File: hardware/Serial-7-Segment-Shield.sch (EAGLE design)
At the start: 28 parts, among them U1 ARDUINO_SHIELDLABEL

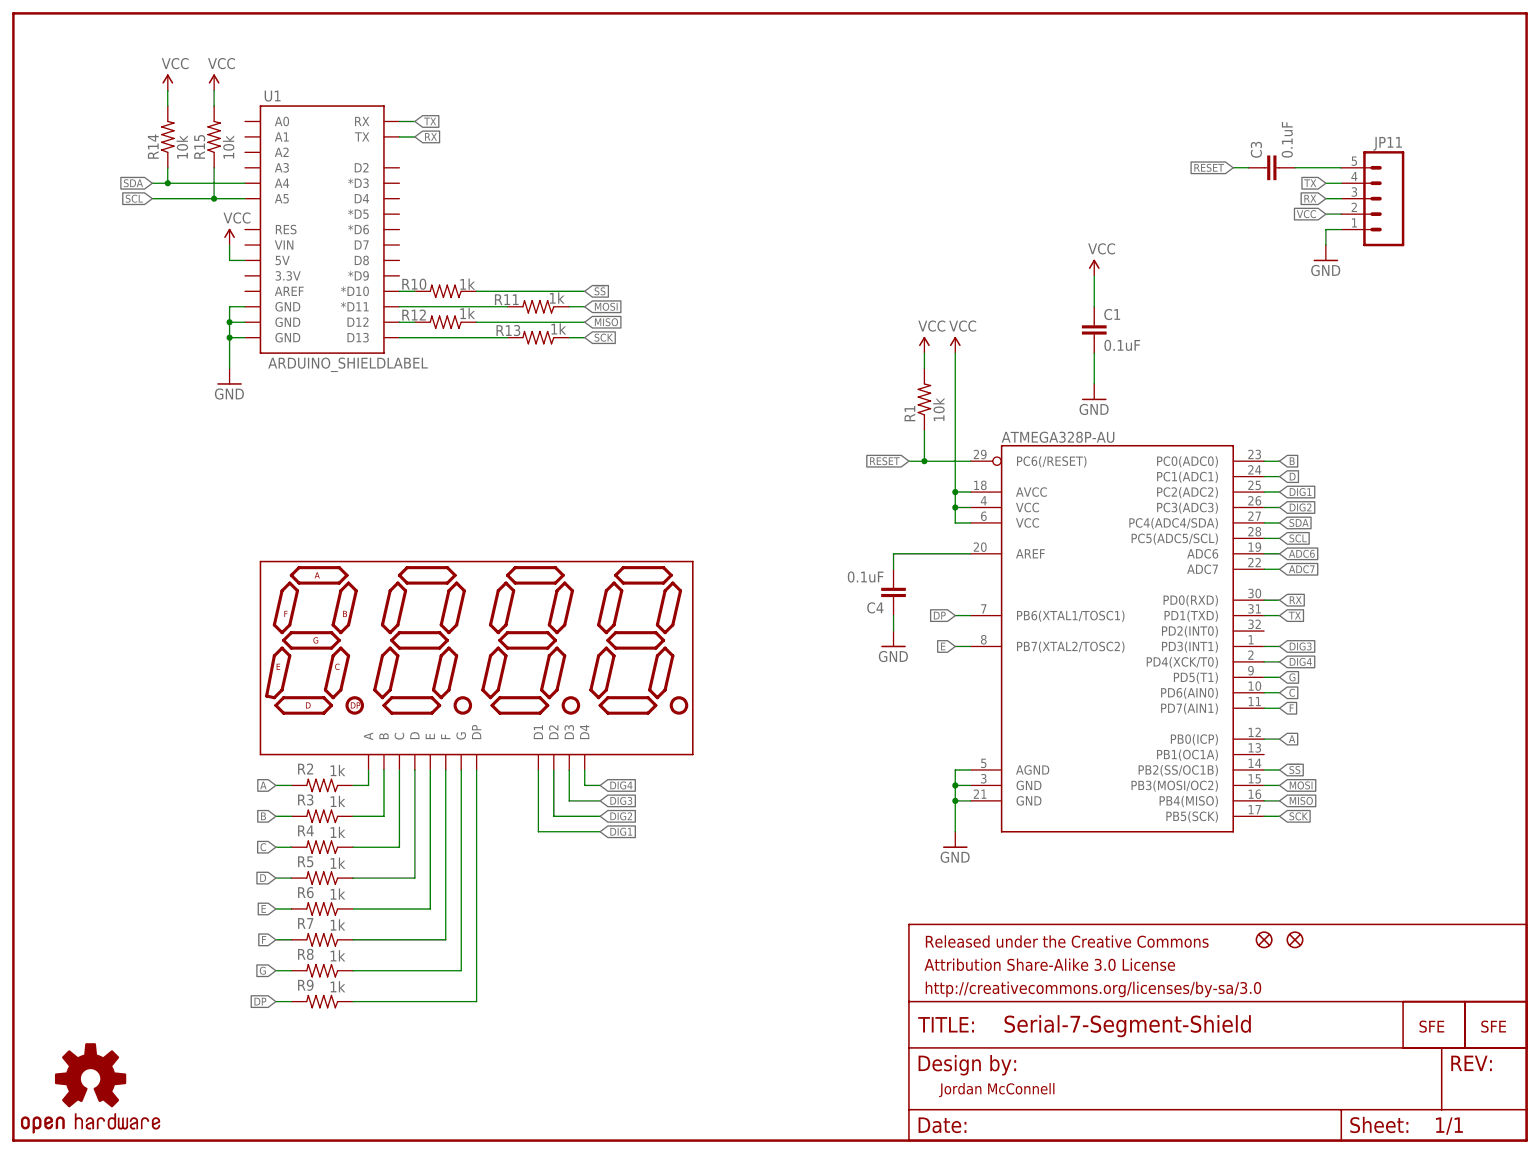
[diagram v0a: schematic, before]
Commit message: Updated hardware to v02.
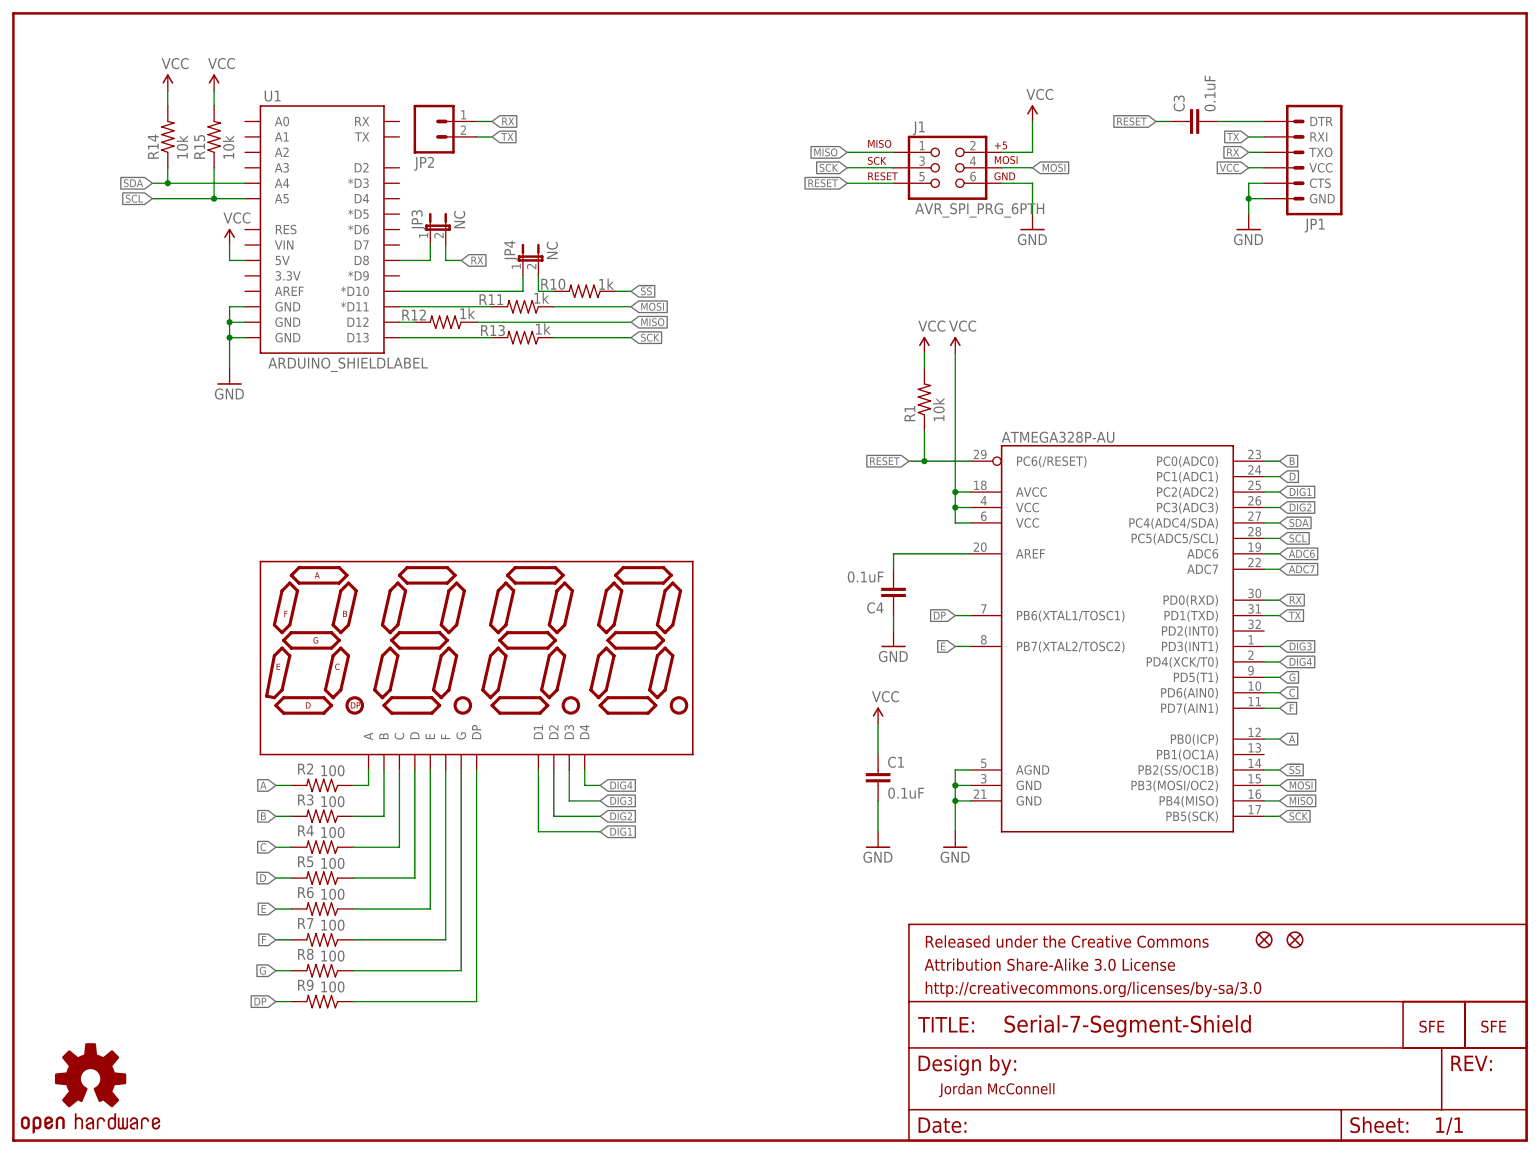
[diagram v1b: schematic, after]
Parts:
- removed JP11: (no value), SparkFun-Connectors:M05PTH-NS
- added J1: AVR_SPI_PRG_6PTH, SparkFun-Connectors:AVR_SPI_PRG_6PTH
- added JP1: (no value), SparkFun-Connectors:ARDUINO_SERIAL_PROGRAMPTH
- added JP2: (no value), SparkFun-Connectors:M02PTH
- added JP3, JP4: NC, SparkFun-Passives:JUMPER-2SMD-NC
- R2, R3, R4, R5, R6, R7, R8, R9: value 1k -> 100
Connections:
- new net N$6: JP4.1, U1.*D10
- new net N$7: JP3.1, U1.D8
- net GND: now also J1.6, JP1.CTS, JP1.GND; no longer JP11.1
- net MISO: now also J1.1
- net MOSI: now also J1.4
- net N$13: now also JP1.DTR; no longer JP11.5
- net N$5: now also JP4.2; no longer U1.*D10
- net RESET: now also J1.5
- net RX: now also JP1.TXO, JP2.1, JP3.2; no longer JP11.3, U1.TX
- net SCK: now also J1.3
- net TX: now also JP1.RXI, JP2.2; no longer JP11.4, U1.RX
- net VCC: now also J1.2, JP1.VCC; no longer JP11.2
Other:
- moved on the sheet: C1, C3, R10, R11, R13

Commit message: Minor update to v02, now includes color selection silk.
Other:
- note added: "v02"
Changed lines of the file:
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@@
 <plain>
 <text x="152.4" y="7.62" size="1.778" layer="94">Jordan McConnell</text>
+<text x="238.76" y="7.62" size="1.778" layer="94">v02</text>
 </plain>
 <instances>

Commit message: v10 Production Ready files
Change version number on boards to v10
Created board panel for manufacture
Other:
- note added: "v10"
- note removed: "v02"
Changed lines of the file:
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@@
 <?xml version="1.0" encoding="utf-8"?>
 <!DOCTYPE eagle SYSTEM "eagle.dtd">
-<eagle version="6.2">
+<eagle version="6.4">
 <drawing>
 <settings>
@@
 <plain>
 <text x="152.4" y="7.62" size="1.778" layer="94">Jordan McConnell</text>
-<text x="238.76" y="7.62" size="1.778" layer="94">v02</text>
+<text x="238.76" y="7.62" size="1.778" layer="94">v10</text>
 </plain>
 <instances>

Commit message: 0603 Cap/Res Change
Changed all caps and res to 0603, minor trace re-routing
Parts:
- C1: device SparkFun:CAP0402-CAP -> SparkFun:CAP0603-CAP
- C3, C4: device SparkFun-Passives:CAP0402-CAP -> SparkFun-Passives:CAP0603-CAP
- R1, R10, R11, R12, R13, R14, R15, R2, R3, R4, R5, R6, R7, R8, R9: device SparkFun:RESISTOR0402-RES -> SparkFun:RESISTOR0603-RES
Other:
- note added: "v11"
- note removed: "v10"
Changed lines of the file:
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@@
 <?xml version="1.0" encoding="utf-8"?>
 <!DOCTYPE eagle SYSTEM "eagle.dtd">
-<eagle version="6.4">
+<eagle version="6.5.0">
 <drawing>
 <settings>
@@
 <layer number="18" name="Vias" color="2" fill="1" visible="no" active="no"/>
 <layer number="19" name="Unrouted" color="6" fill="1" visible="no" active="no"/>
-<layer number="20" name="Dimension" color="15" fill="1" visible="no" active="no"/>
-<layer number="21" name="tPlace" color="16" fill="1" visible="no" active="no"/>
-<layer number="22" name="bPlace" color="14" fill="1" visible="no" active="no"/>
+<layer number="20" name="Dimension" color="6" fill="1" visible="no" active="no"/>
+<layer number="21" name="tPlace" color="6" fill="1" visible="no" active="no"/>
+<layer number="22" name="bPlace" color="6" fill="1" visible="no" active="no"/>
 <layer number="23" name="tOrigins" color="15" fill="1" visible="no" active="no"/>
 <layer number="24" name="bOrigins" color="15" fill="1" visible="no" active="no"/>
@@
 <part name="GND1" library="SparkFun" deviceset="GND" device=""/>
 <part name="P+2" library="SparkFun" deviceset="VCC" device=""/>
-<part name="R1" library="SparkFun" deviceset="RESISTOR" device="0402-RES" value="10k"/>
-<part name="C1" library="SparkFun" deviceset="CAP" device="0402-CAP" value="0.1uF"/>
+<part name="R1" library="SparkFun" deviceset="RESISTOR" device="0603-RES" value="10k"/>
+<part name="C1" library="SparkFun" deviceset="CAP" device="0603-CAP" value="0.1uF"/>
 <part name="P+3" library="SparkFun" deviceset="VCC" device=""/>
 <part name="GND4" library="SparkFun" deviceset="GND" device=""/>
 <part name="GND7" library="SparkFun-Aesthetics" deviceset="GND" device=""/>
-<part name="C3" library="SparkFun-Passives" deviceset="CAP" device="0402-CAP" value="0.1uF"/>
+<part name="C3" library="SparkFun-Passives" deviceset="CAP" device="0603-CAP" value="0.1uF"/>
 <part name="U$4" library="SparkFun-Aesthetics" deviceset="OSHW-LOGO" device="S"/>
-<part name="C4" library="SparkFun-Passives" deviceset="CAP" device="0402-CAP" value="0.1uF"/>
+<part name="C4" library="SparkFun-Passives" deviceset="CAP" device="0603-CAP" value="0.1uF"/>
 <part name="GND2" library="SparkFun" deviceset="GND" device=""/>
 <part name="JP9" library="SparkFun" deviceset="FIDUCIAL" device="UFIDUCIAL"/>
@@
 <part name="LOGO2" library="SparkFun-Aesthetics" deviceset="LOGO-SFE" device="NEW"/>
 <part name="U$1" library="SparkFun-Displays" deviceset="7-SEGMENT-4DIGIT-COUNTER" device="PTH"/>
-<part name="R2" library="SparkFun" deviceset="RESISTOR" device="0402-RES" value="100"/>
-<part name="R3" library="SparkFun" deviceset="RESISTOR" device="0402-RES" value="100"/>
-<part name="R4" library="SparkFun" deviceset="RESISTOR" device="0402-RES" value="100"/>
-<part name="R5" library="SparkFun" deviceset="RESISTOR" device="0402-RES" value="100"/>
-<part name="R6" library="SparkFun" deviceset="RESISTOR" device="0402-RES" value="100"/>
-<part name="R7" library="SparkFun" deviceset="RESISTOR" device="0402-RES" value="100"/>
-<part name="R8" library="SparkFun" deviceset="RESISTOR" device="0402-RES" value="100"/>
-<part name="R9" library="SparkFun" deviceset="RESISTOR" device="0402-RES" value="100"/>
-<part name="R10" library="SparkFun" deviceset="RESISTOR" device="0402-RES" value="1k"/>
-<part name="R11" library="SparkFun" deviceset="RESISTOR" device="0402-RES" value="1k"/>
-<part name="R12" library="SparkFun" deviceset="RESISTOR" device="0402-RES" value="1k"/>
-<part name="R13" library="SparkFun" deviceset="RESISTOR" device="0402-RES" value="1k"/>
-<part name="R14" library="SparkFun" deviceset="RESISTOR" device="0402-RES" value="10k"/>
-<part name="R15" library="SparkFun" deviceset="RESISTOR" device="0402-RES" value="10k"/>
+<part name="R2" library="SparkFun" deviceset="RESISTOR" device="0603-RES" value="100"/>
+<part name="R3" library="SparkFun" deviceset="RESISTOR" device="0603-RES" value="100"/>
+<part name="R4" library="SparkFun" deviceset="RESISTOR" device="0603-RES" value="100"/>
+<part name="R5" library="SparkFun" deviceset="RESISTOR" device="0603-RES" value="100"/>
+<part name="R6" library="SparkFun" deviceset="RESISTOR" device="0603-RES" value="100"/>
+<part name="R7" library="SparkFun" deviceset="RESISTOR" device="0603-RES" value="100"/>
+<part name="R8" library="SparkFun" deviceset="RESISTOR" device="0603-RES" value="100"/>
+<part name="R9" library="SparkFun" deviceset="RESISTOR" device="0603-RES" value="100"/>
+<part name="R10" library="SparkFun" deviceset="RESISTOR" device="0603-RES" value="1k"/>
+<part name="R11" library="SparkFun" deviceset="RESISTOR" device="0603-RES" value="1k"/>
+<part name="R12" library="SparkFun" deviceset="RESISTOR" device="0603-RES" value="1k"/>
+<part name="R13" library="SparkFun" deviceset="RESISTOR" device="0603-RES" value="1k"/>
+<part name="R14" library="SparkFun" deviceset="RESISTOR" device="0603-RES" value="10k"/>
+<part name="R15" library="SparkFun" deviceset="RESISTOR" device="0603-RES" value="10k"/>
 <part name="P+4" library="SparkFun" deviceset="VCC" device=""/>
 <part name="P+5" library="SparkFun" deviceset="VCC" device=""/>
@@
 <plain>
 <text x="152.4" y="7.62" size="1.778" layer="94">Jordan McConnell</text>
-<text x="238.76" y="7.62" size="1.778" layer="94">v10</text>
+<text x="238.76" y="7.62" size="1.778" layer="94">v11</text>
 </plain>
 <instances>

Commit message: commit to QC branch
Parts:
- U1: value ARDUINO_SHIELDLABEL -> ARDUINO_R3_SHIELD; device SparkFun-Boards:ARDUINO_SHIELDLABEL -> SparkFun-Boards:ARDUINO_R3_SHIELD
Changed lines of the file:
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@@
 <?xml version="1.0" encoding="utf-8"?>
 <!DOCTYPE eagle SYSTEM "eagle.dtd">
-<eagle version="6.5.0">
+<eagle version="6.4">
 <drawing>
 <settings>
@@
 <part name="JP9" library="SparkFun" deviceset="FIDUCIAL" device="UFIDUCIAL"/>
 <part name="JP10" library="SparkFun" deviceset="FIDUCIAL" device="UFIDUCIAL"/>
-<part name="U1" library="SparkFun-Boards" deviceset="ARDUINO_SHIELD" device="LABEL"/>
+<part name="U1" library="SparkFun-Boards" deviceset="ARDUINO_R3_SHIELD" device=""/>
 <part name="GND5" library="SparkFun" deviceset="GND" device=""/>
 <part name="P+6" library="SparkFun" deviceset="VCC" device=""/>
@@
 <instance part="JP10" gate="G$1" x="210.82" y="33.02"/>
 <instance part="U1" gate="G$1" x="50.8" y="149.86"/>
-<instance part="GND5" gate="1" x="35.56" y="124.46"/>
+<instance part="GND5" gate="1" x="35.56" y="119.38"/>
 <instance part="P+6" gate="1" x="35.56" y="147.32"/>
 <instance part="LOGO1" gate="G$1" x="241.3" y="17.78"/>
@@
 <segment>
 <pinref part="U1" gate="G$1" pin="5V"/>
-<wire x1="38.1" y1="144.78" x2="35.56" y2="144.78" width="0.1524" layer="91"/>
+<wire x1="38.1" y1="139.7" x2="35.56" y2="139.7" width="0.1524" layer="91"/>
 <pinref part="P+6" gate="1" pin="VCC"/>
-<wire x1="35.56" y1="144.78" x2="35.56" y2="147.32" width="0.1524" layer="91"/>
+<wire x1="35.56" y1="139.7" x2="35.56" y2="147.32" width="0.1524" layer="91"/>
 </segment>
 <segment>
@@
 <segment>
 <pinref part="GND5" gate="1" pin="GND"/>
-<wire x1="35.56" y1="127" x2="35.56" y2="132.08" width="0.1524" layer="91"/>
+<wire x1="35.56" y1="121.92" x2="35.56" y2="127" width="0.1524" layer="91"/>
 <pinref part="U1" gate="G$1" pin="GND@0"/>
+<wire x1="35.56" y1="127" x2="38.1" y2="127" width="0.1524" layer="91"/>
+<wire x1="35.56" y1="127" x2="35.56" y2="129.54" width="0.1524" layer="91"/>
+<junction x="35.56" y="127"/>
+<pinref part="U1" gate="G$1" pin="GND@1"/>
+<wire x1="35.56" y1="129.54" x2="38.1" y2="129.54" width="0.1524" layer="91"/>
+<wire x1="35.56" y1="129.54" x2="35.56" y2="132.08" width="0.1524" layer="91"/>
+<junction x="35.56" y="129.54"/>
+<pinref part="U1" gate="G$1" pin="GND@2"/>
 <wire x1="35.56" y1="132.08" x2="38.1" y2="132.08" width="0.1524" layer="91"/>
-<wire x1="35.56" y1="132.08" x2="35.56" y2="134.62" width="0.1524" layer="91"/>
-<junction x="35.56" y="132.08"/>
-<pinref part="U1" gate="G$1" pin="GND@1"/>
-<wire x1="35.56" y1="134.62" x2="38.1" y2="134.62" width="0.1524" layer="91"/>
-<wire x1="35.56" y1="134.62" x2="35.56" y2="137.16" width="0.1524" layer="91"/>
-<junction x="35.56" y="134.62"/>
-<pinref part="U1" gate="G$1" pin="GND@2"/>
-<wire x1="35.56" y1="137.16" x2="38.1" y2="137.16" width="0.1524" layer="91"/>
-</segment>
-<segment>
+</segment>
+<segment>

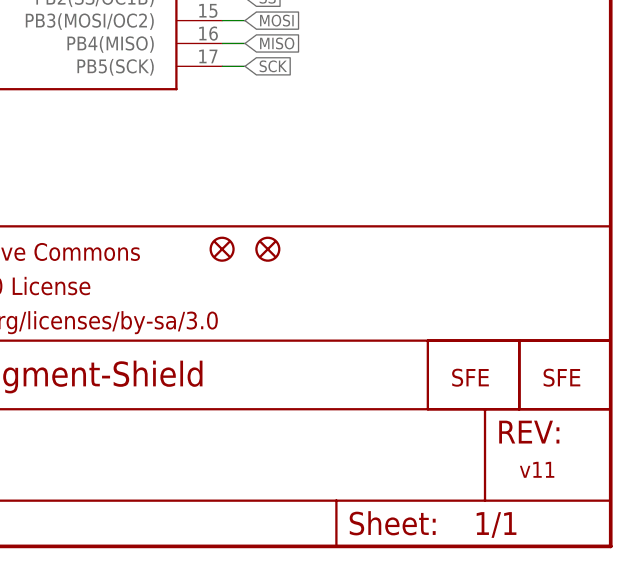
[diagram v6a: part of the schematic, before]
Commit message: changed micro fid to regular
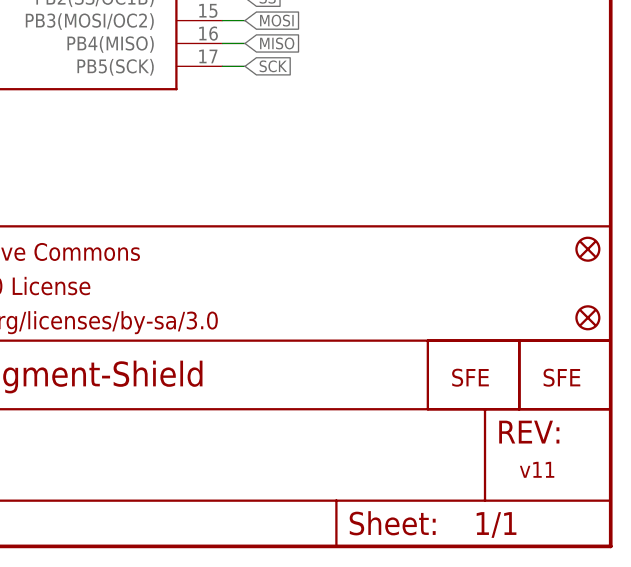
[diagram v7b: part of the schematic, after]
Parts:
- removed JP10, JP9: FIDUCIALUFIDUCIAL, SparkFun:FIDUCIALUFIDUCIAL
- added FID1, FID2: FIDUCIAL1X2, SparkFun-Aesthetics:FIDUCIAL1X2
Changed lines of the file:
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@@
 <?xml version="1.0" encoding="utf-8"?>
 <!DOCTYPE eagle SYSTEM "eagle.dtd">
-<eagle version="6.4">
+<eagle version="6.5.0">
 <drawing>
 <settings>
@@
 <part name="C4" library="SparkFun-Passives" deviceset="CAP" device="0603-CAP" value="0.1uF"/>
 <part name="GND2" library="SparkFun" deviceset="GND" device=""/>
-<part name="JP9" library="SparkFun" deviceset="FIDUCIAL" device="UFIDUCIAL"/>
-<part name="JP10" library="SparkFun" deviceset="FIDUCIAL" device="UFIDUCIAL"/>
 <part name="U1" library="SparkFun-Boards" deviceset="ARDUINO_R3_SHIELD" device=""/>
 <part name="GND5" library="SparkFun" deviceset="GND" device=""/>
@@
 <part name="JP3" library="SparkFun-Passives" deviceset="JUMPER-2" device="SMD-NC" value="NC"/>
 <part name="JP4" library="SparkFun-Passives" deviceset="JUMPER-2" device="SMD-NC" value="NC"/>
+<part name="FID1" library="SparkFun-Aesthetics" deviceset="FIDUCIAL" device="1X2"/>
+<part name="FID2" library="SparkFun-Aesthetics" deviceset="FIDUCIAL" device="1X2"/>
 </parts>
 <sheets>
@@
 <instance part="C4" gate="G$1" x="144.78" y="91.44" rot="R180"/>
 <instance part="GND2" gate="1" x="144.78" y="81.28"/>
-<instance part="JP9" gate="G$1" x="205.74" y="33.02"/>
-<instance part="JP10" gate="G$1" x="210.82" y="33.02"/>
 <instance part="U1" gate="G$1" x="50.8" y="149.86"/>
 <instance part="GND5" gate="1" x="35.56" y="119.38"/>
@@
 <instance part="JP3" gate="A" x="68.58" y="149.86"/>
 <instance part="JP4" gate="A" x="83.82" y="144.78"/>
+<instance part="FID1" gate="G$1" x="246.38" y="33.02"/>
+<instance part="FID2" gate="G$1" x="246.38" y="25.4"/>
 </instances>
 <busses>
